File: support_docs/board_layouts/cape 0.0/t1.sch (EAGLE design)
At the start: 8 parts, among them IC1 74HC595N, X1 332-46, X2 332-46

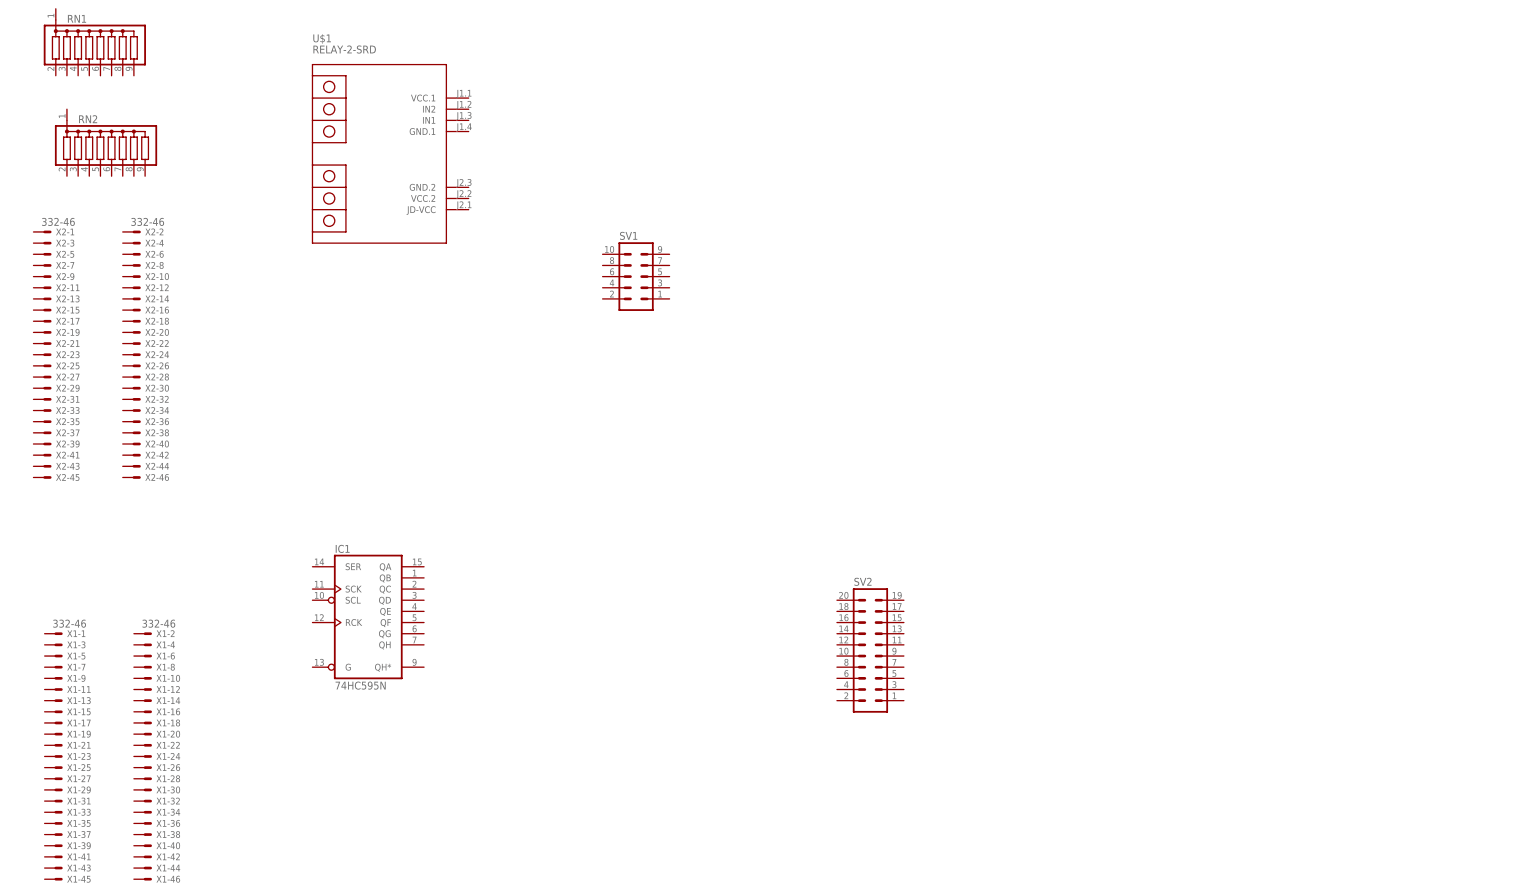
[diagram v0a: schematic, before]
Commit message: add list maint code
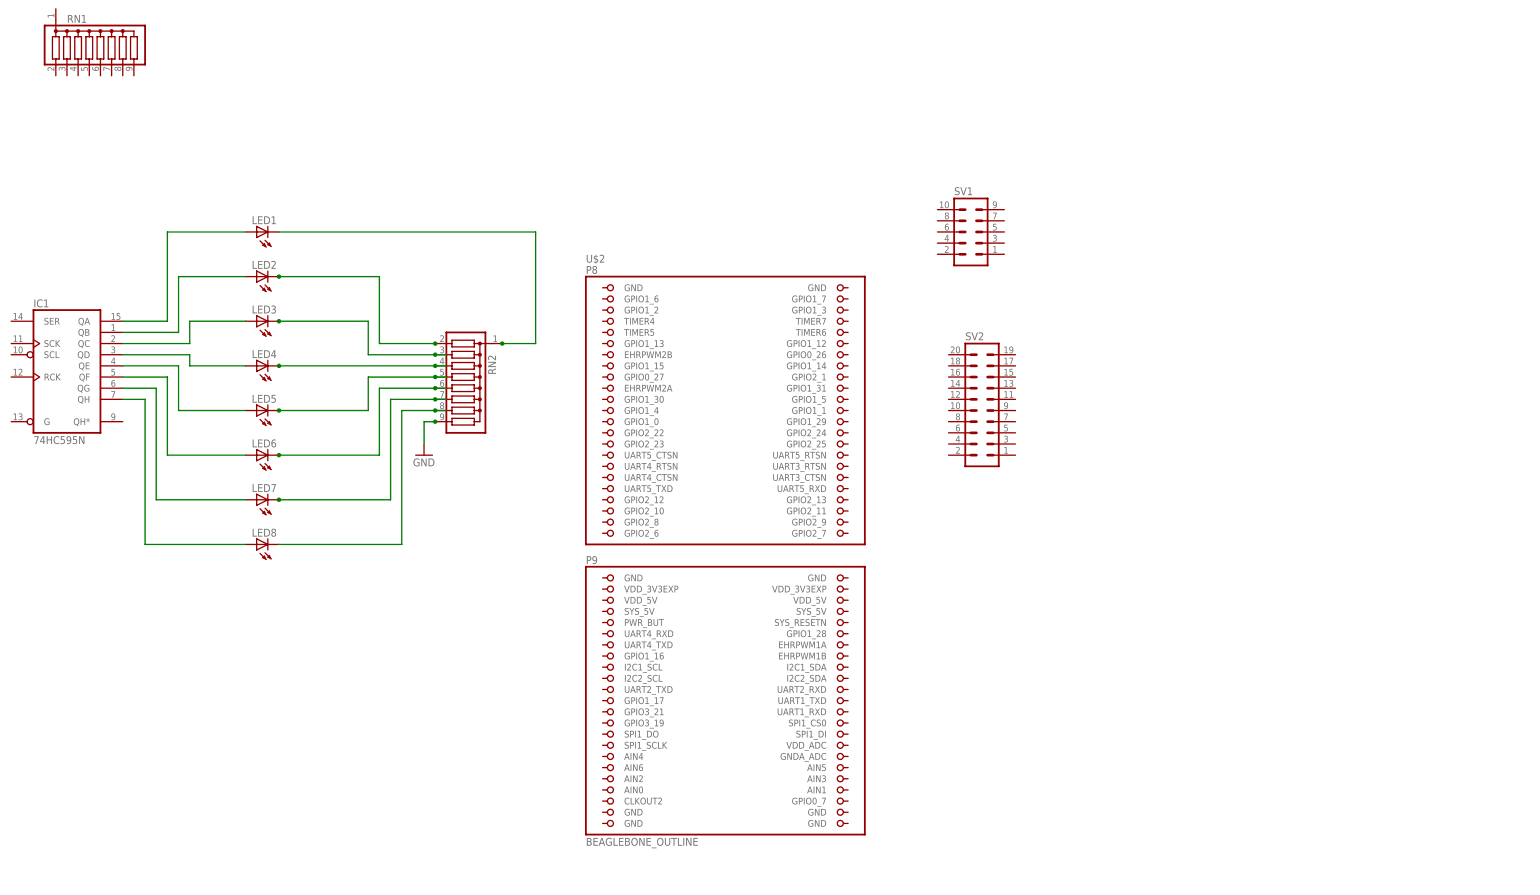
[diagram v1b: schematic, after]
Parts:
- removed U$1: RELAY-2-SRD, diy-modules:RELAY-2-SRD
- removed X1, X2: 332-46, con-garry:332-46
- added LED1, LED2, LED3, LED4, LED5, LED6, LED7, LED8: (no value), adafruit:LED3MM
- added U$2: BEAGLEBONE_OUTLINE, local:BEAGLEBONE_OUTLINE
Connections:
- new net GND: RN2.9
- new net N$1: LED1.C, RN2.1
- new net N$10: IC1A.QB, LED2.A
- new net N$11: IC1A.QC, LED3.A
- new net N$12: IC1A.QD, LED4.A
- new net N$13: IC1A.QE, LED5.A
- new net N$14: IC1A.QF, LED6.A
- new net N$15: IC1A.QG, LED7.A
- new net N$16: IC1A.QH, LED8.A
- new net N$2: LED2.C, RN2.2
- new net N$3: LED3.C, RN2.3
- new net N$4: LED4.C, RN2.4
- new net N$5: LED5.C, RN2.5
- new net N$6: LED6.C, RN2.6
- new net N$7: LED7.C, RN2.7
- new net N$8: LED8.C, RN2.8
- new net N$9: IC1A.QA, LED1.A
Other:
- moved on the sheet: IC1, RN2, SV1, SV2

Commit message: testing and updating cape layout
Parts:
- removed U$2: BEAGLEBONE_OUTLINE, local:BEAGLEBONE_OUTLINE
- added BBB: BEAGLEBONE_OUTLINE, local:BEAGLEBONE_OUTLINE
- added LED0: (no value), adafruit:LED3MM
- added R1: 10k, rcl:R-US_0207/12
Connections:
- removed net N$1: LED1.C, RN2.1
- new net +3V3: IC1P.VCC, R1.2
- new net /OE_RLY: IC1A.G, R1.1
- new net DATA_RLY: BBB.GPIO1_13, IC1A.SER
- new net N$17: IC1A.QH, LED7.A
- net GND: now also BBB.GND@1, BBB.GND@2, BBB.GND@3, BBB.GND@4, BBB.GND@5, BBB.GND@6, BBB.GND@7, BBB.GND@8, IC1P.GND, RN2.1; no longer RN2.9
- net N$10: now also LED5.C, RN2.7; no longer IC1A.QB, LED2.A
- net N$11: now also LED2.A; no longer LED3.A
- net N$12: now also LED3.A; no longer LED4.A
- net N$13: now also LED4.A; no longer LED5.A
- net N$14: now also LED5.A; no longer LED6.A
- net N$15: now also LED7.C, RN2.9; no longer IC1A.QG, LED7.A
- net N$16: now also IC1A.QG, LED6.A; no longer IC1A.QH, LED8.A
- net N$2: now also LED1.C, RN2.3; no longer LED2.C, RN2.2
- net N$3: now also RN2.5; no longer RN2.3
- net N$4: now also LED2.C; no longer LED4.C
- net N$5: now also LED4.C, RN2.6; no longer LED5.C, RN2.5
- net N$6: now also RN2.8; no longer RN2.6
- net N$7: now also LED0.C, RN2.2; no longer LED7.C, RN2.7
- net N$8: now also IC1A.QA, LED0.A; no longer LED8.C, RN2.8
- net N$9: now also IC1A.QB; no longer IC1A.QA
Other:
- moved on the sheet: IC1, LED1, LED2, LED3, LED4, LED5, LED6, LED7, LED8, RN1, RN2, SV1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

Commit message: working on cape layout
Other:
- moved on the sheet: RN2
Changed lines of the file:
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@@
 <instances>
 <instance part="RN1" gate="G$1" x="71.12" y="149.86"/>
-<instance part="RN2" gate="G$1" x="152.4" y="73.66" rot="R270"/>
+<instance part="RN2" gate="G$1" x="154.94" y="73.66" rot="R270"/>
 <instance part="IC1" gate="A" x="73.66" y="78.74"/>
 <instance part="SV1" gate="G$1" x="269.24" y="109.22"/>
@@
 <segment>
 <pinref part="RN2" gate="G$1" pin="4"/>
-<wire x1="147.32" y1="78.74" x2="149.86" y2="78.74" width="0.1524" layer="91"/>
 <pinref part="LED2" gate="G$1" pin="C"/>
 <wire x1="124.46" y1="88.9" x2="137.16" y2="88.9" width="0.1524" layer="91"/>
 <wire x1="137.16" y1="88.9" x2="137.16" y2="78.74" width="0.1524" layer="91"/>
-<wire x1="137.16" y1="78.74" x2="147.32" y2="78.74" width="0.1524" layer="91"/>
-<junction x="147.32" y="78.74"/>
+<wire x1="137.16" y1="78.74" x2="149.86" y2="78.74" width="0.1524" layer="91"/>
 </segment>
 </net>
@@
 <segment>
 <pinref part="RN2" gate="G$1" pin="3"/>
-<wire x1="147.32" y1="81.28" x2="149.86" y2="81.28" width="0.1524" layer="91"/>
 <pinref part="LED1" gate="G$1" pin="C"/>
 <wire x1="124.46" y1="99.06" x2="139.7" y2="99.06" width="0.1524" layer="91"/>
 <wire x1="139.7" y1="99.06" x2="139.7" y2="81.28" width="0.1524" layer="91"/>
-<wire x1="139.7" y1="81.28" x2="147.32" y2="81.28" width="0.1524" layer="91"/>
-<junction x="147.32" y="81.28"/>
+<wire x1="139.7" y1="81.28" x2="149.86" y2="81.28" width="0.1524" layer="91"/>
 </segment>
 </net>
@@
 <segment>
 <pinref part="RN2" gate="G$1" pin="5"/>
-<wire x1="147.32" y1="76.2" x2="149.86" y2="76.2" width="0.1524" layer="91"/>
 <pinref part="LED3" gate="G$1" pin="C"/>
 <wire x1="124.46" y1="78.74" x2="134.62" y2="78.74" width="0.1524" layer="91"/>
 <wire x1="134.62" y1="78.74" x2="134.62" y2="76.2" width="0.1524" layer="91"/>
-<wire x1="134.62" y1="76.2" x2="147.32" y2="76.2" width="0.1524" layer="91"/>
-<junction x="147.32" y="76.2"/>
+<wire x1="134.62" y1="76.2" x2="149.86" y2="76.2" width="0.1524" layer="91"/>
 </segment>
 </net>
@@
 <segment>
 <pinref part="RN2" gate="G$1" pin="6"/>
-<wire x1="147.32" y1="73.66" x2="149.86" y2="73.66" width="0.1524" layer="91"/>
 <pinref part="LED4" gate="G$1" pin="C"/>
 <wire x1="124.46" y1="68.58" x2="134.62" y2="68.58" width="0.1524" layer="91"/>
 <wire x1="134.62" y1="68.58" x2="134.62" y2="73.66" width="0.1524" layer="91"/>
-<wire x1="134.62" y1="73.66" x2="147.32" y2="73.66" width="0.1524" layer="91"/>
-<junction x="147.32" y="73.66"/>
+<wire x1="134.62" y1="73.66" x2="149.86" y2="73.66" width="0.1524" layer="91"/>
 </segment>
 </net>
@@
 <segment>
 <pinref part="RN2" gate="G$1" pin="8"/>
-<wire x1="147.32" y1="68.58" x2="149.86" y2="68.58" width="0.1524" layer="91"/>
 <pinref part="LED6" gate="G$1" pin="C"/>
 <wire x1="124.46" y1="48.26" x2="139.7" y2="48.26" width="0.1524" layer="91"/>
 <wire x1="139.7" y1="48.26" x2="139.7" y2="68.58" width="0.1524" layer="91"/>
-<wire x1="139.7" y1="68.58" x2="147.32" y2="68.58" width="0.1524" layer="91"/>
-<junction x="147.32" y="68.58"/>
+<wire x1="139.7" y1="68.58" x2="149.86" y2="68.58" width="0.1524" layer="91"/>
 </segment>
 </net>
@@
 <segment>
 <pinref part="RN2" gate="G$1" pin="7"/>
-<wire x1="147.32" y1="71.12" x2="149.86" y2="71.12" width="0.1524" layer="91"/>
 <pinref part="LED5" gate="G$1" pin="C"/>
 <wire x1="124.46" y1="58.42" x2="137.16" y2="58.42" width="0.1524" layer="91"/>
 <wire x1="137.16" y1="58.42" x2="137.16" y2="71.12" width="0.1524" layer="91"/>
-<wire x1="137.16" y1="71.12" x2="147.32" y2="71.12" width="0.1524" layer="91"/>
-<junction x="147.32" y="71.12"/>
+<wire x1="137.16" y1="71.12" x2="149.86" y2="71.12" width="0.1524" layer="91"/>
 </segment>
 </net>
@@
 <pinref part="RN2" gate="G$1" pin="1"/>
 <pinref part="GND1" gate="1" pin="GND"/>
-<wire x1="162.56" y1="83.82" x2="167.64" y2="83.82" width="0.1524" layer="91"/>
+<wire x1="165.1" y1="83.82" x2="167.64" y2="83.82" width="0.1524" layer="91"/>
 <wire x1="167.64" y1="83.82" x2="167.64" y2="81.28" width="0.1524" layer="91"/>
 </segment>
@@
 </segment>
 </net>
-<net name="N$15" class="0">
-<segment>
-<pinref part="LED7" gate="G$1" pin="C"/>
-<wire x1="124.46" y1="38.1" x2="142.24" y2="38.1" width="0.1524" layer="91"/>
-<wire x1="142.24" y1="38.1" x2="142.24" y2="66.04" width="0.1524" layer="91"/>
-<pinref part="RN2" gate="G$1" pin="9"/>
-<wire x1="142.24" y1="66.04" x2="147.32" y2="66.04" width="0.1524" layer="91"/>
-</segment>
-</net>
 <net name="N$7" class="0">
 <segment>
 <pinref part="RN2" gate="G$1" pin="2"/>
-<wire x1="147.32" y1="83.82" x2="142.24" y2="83.82" width="0.1524" layer="91"/>
+<wire x1="149.86" y1="83.82" x2="142.24" y2="83.82" width="0.1524" layer="91"/>
 <wire x1="142.24" y1="83.82" x2="142.24" y2="109.22" width="0.1524" layer="91"/>
 <pinref part="LED0" gate="G$1" pin="C"/>
@@
 </segment>
 </net>
+<net name="N$1" class="0">
+<segment>
+<pinref part="LED7" gate="G$1" pin="C"/>
+<wire x1="124.46" y1="38.1" x2="142.24" y2="38.1" width="0.1524" layer="91"/>
+<wire x1="142.24" y1="38.1" x2="142.24" y2="66.04" width="0.1524" layer="91"/>
+<pinref part="RN2" gate="G$1" pin="9"/>
+<wire x1="149.86" y1="66.04" x2="142.24" y2="66.04" width="0.1524" layer="91"/>
+</segment>
+</net>
